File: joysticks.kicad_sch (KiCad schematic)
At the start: 27 parts, among them J1 DB9_Male_MountingHoles, J2 DB9_Male_MountingHoles, J25 Joystick Ports Mezannine Lower, J26 Joystick Ports Mezannine Upper, SW1 SW_Push_DPDT, U10 74LS06N, U11 74LS06N, U5 74LS06N, U6 74LVC374, U7 74LVC374, U8 74LS373, U9 74LS373

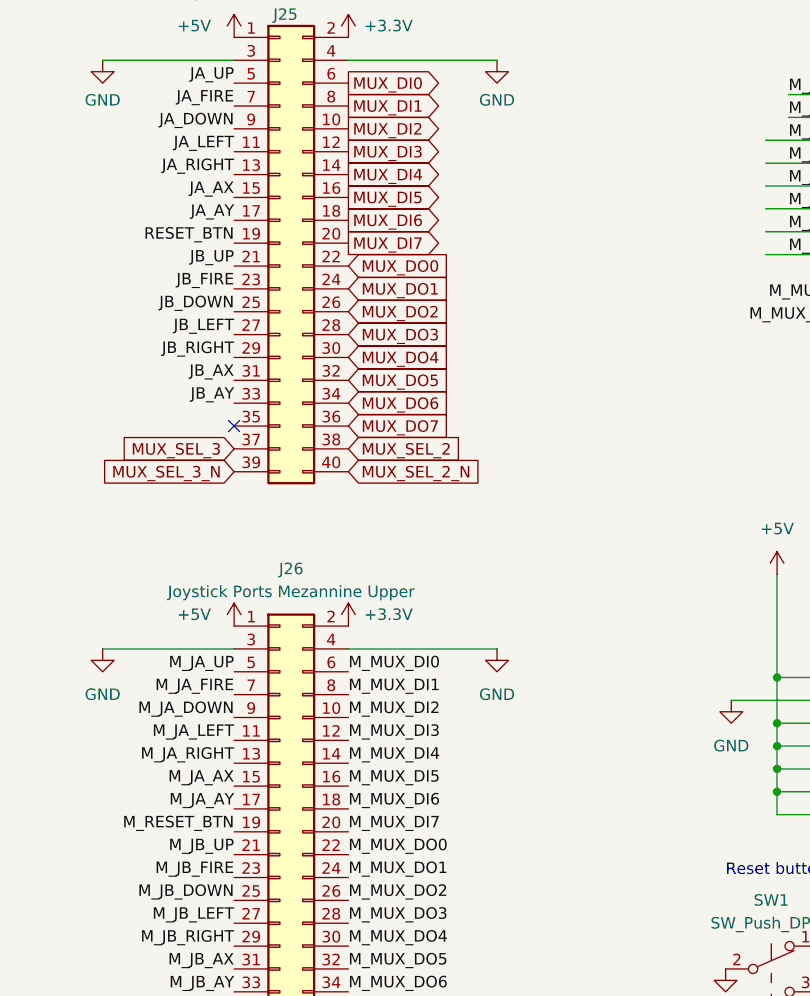
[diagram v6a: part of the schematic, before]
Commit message: finish laying out joystick mezzannine PCB
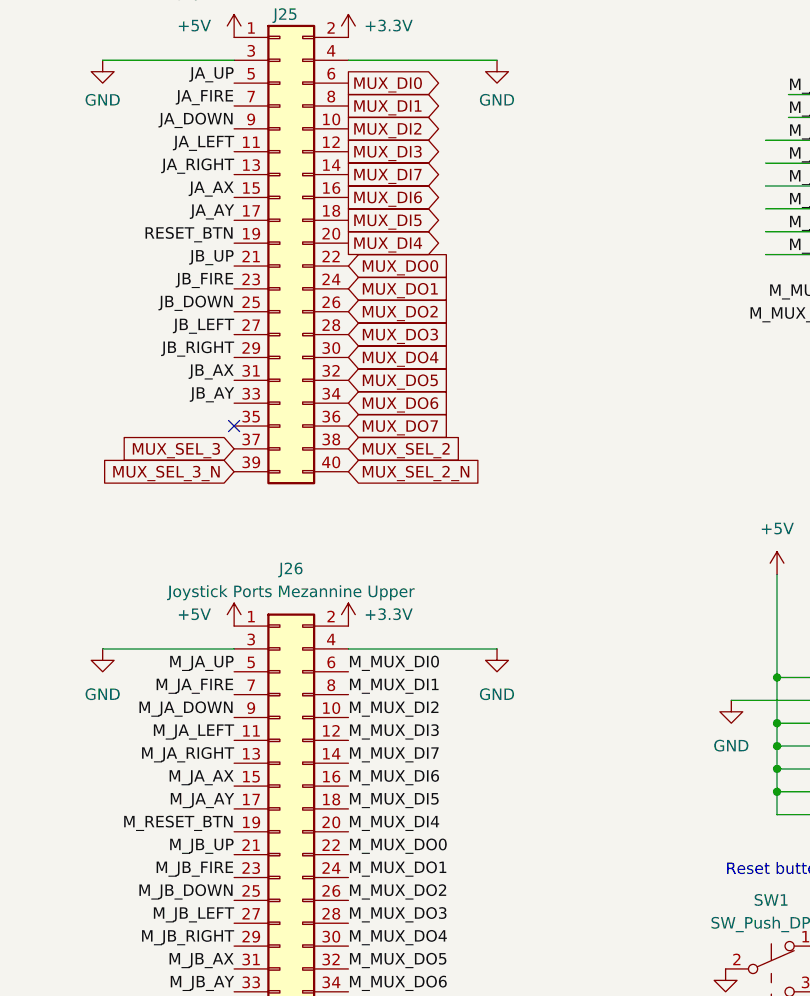
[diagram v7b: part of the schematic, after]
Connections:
- net MUX_DI4: now also J25.20 (Pin_20); no longer J25.14 (Pin_14)
- net MUX_DI5: now also J25.18 (Pin_18); no longer J25.16 (Pin_16)
- net MUX_DI6: now also J25.16 (Pin_16); no longer J25.18 (Pin_18)
- net MUX_DI7: now also J25.14 (Pin_14); no longer J25.20 (Pin_20)
- net M_MUX_DI4: now also J26.20 (Pin_20); no longer J26.14 (Pin_14)
- net M_MUX_DI5: now also J26.18 (Pin_18); no longer J26.16 (Pin_16)
- net M_MUX_DI6: now also J26.16 (Pin_16); no longer J26.18 (Pin_18)
- net M_MUX_DI7: now also J26.14 (Pin_14); no longer J26.20 (Pin_20)
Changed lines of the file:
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@@
     (effects (font (size 1.27 1.27)) (justify left bottom))
   )
-  (label "M_MUX_DI6" (at 62.23 106.68 0)
+  (label "M_MUX_DI6" (at 62.23 104.14 0)
     (effects (font (size 1.27 1.27)) (justify left bottom))
   )
@@
     (effects (font (size 1.27 1.27)) (justify left bottom))
   )
-  (label "M_MUX_DI7" (at 62.23 109.22 0)
+  (label "M_MUX_DI7" (at 62.23 101.6 0)
     (effects (font (size 1.27 1.27)) (justify left bottom))
   )
@@
     (effects (font (size 1.27 1.27)) (justify right bottom))
   )
-  (label "M_MUX_DI4" (at 62.23 101.6 0)
+  (label "M_MUX_DI4" (at 62.23 109.22 0)
     (effects (font (size 1.27 1.27)) (justify left bottom))
   )
@@
     (effects (font (size 1.27 1.27)) (justify left bottom))
   )
-  (label "M_MUX_DI5" (at 62.23 104.14 0)
+  (label "M_MUX_DI5" (at 62.23 106.68 0)
     (effects (font (size 1.27 1.27)) (justify left bottom))
   )
@@
     )
   )
-  (global_label "MUX_DI4" (shape output) (at 62.23 36.195 0) (fields_autoplaced)
-    (effects (font (size 1.27 1.27)) (justify left))
-    (property "Intersheet References" "${INTERSHEET_REFS}" (id 0) (at 72.6864 36.1156 0)
+  (global_label "MUX_DI4" (shape output) (at 62.23 43.815 0) (fields_autoplaced)
+    (effects (font (size 1.27 1.27)) (justify left))
+    (property "Intersheet References" "${INTERSHEET_REFS}" (id 0) (at 72.6864 43.8944 0)
       (effects (font (size 1.27 1.27)) (justify left) hide)
     )
@@
     )
   )
-  (global_label "MUX_DI7" (shape output) (at 62.23 43.815 0) (fields_autoplaced)
-    (effects (font (size 1.27 1.27)) (justify left))
-    (property "Intersheet References" "${INTERSHEET_REFS}" (id 0) (at 72.6864 43.7356 0)
+  (global_label "MUX_DI7" (shape output) (at 62.23 36.195 0) (fields_autoplaced)
+    (effects (font (size 1.27 1.27)) (justify left))
+    (property "Intersheet References" "${INTERSHEET_REFS}" (id 0) (at 72.6864 36.2744 0)
       (effects (font (size 1.27 1.27)) (justify left) hide)
     )
@@
     )
   )
-  (global_label "MUX_DI6" (shape output) (at 62.23 41.275 0) (fields_autoplaced)
-    (effects (font (size 1.27 1.27)) (justify left))
-    (property "Intersheet References" "${INTERSHEET_REFS}" (id 0) (at 72.6864 41.1956 0)
+  (global_label "MUX_DI6" (shape output) (at 62.23 38.735 0) (fields_autoplaced)
+    (effects (font (size 1.27 1.27)) (justify left))
+    (property "Intersheet References" "${INTERSHEET_REFS}" (id 0) (at 72.6864 38.8144 0)
       (effects (font (size 1.27 1.27)) (justify left) hide)
     )
@@
     )
   )
-  (global_label "MUX_DI5" (shape output) (at 62.23 38.735 0) (fields_autoplaced)
-    (effects (font (size 1.27 1.27)) (justify left))
-    (property "Intersheet References" "${INTERSHEET_REFS}" (id 0) (at 72.6864 38.6556 0)
-      (effects (font (size 1.27 1.27)) (justify left) hide)
-    )
+  (global_label "MUX_DI5" (shape output) (at 62.23 41.275 0) (fields_autoplaced)
+    (effects (font (size 1.27 1.27)) (justify left))
+    (property "Intersheet References" "${INTERSHEET_REFS}" (id 0) (at 72.6864 41.3544 0)
+      (effects (font (size 1.27 1.27)) (justify left) hide)
+    )

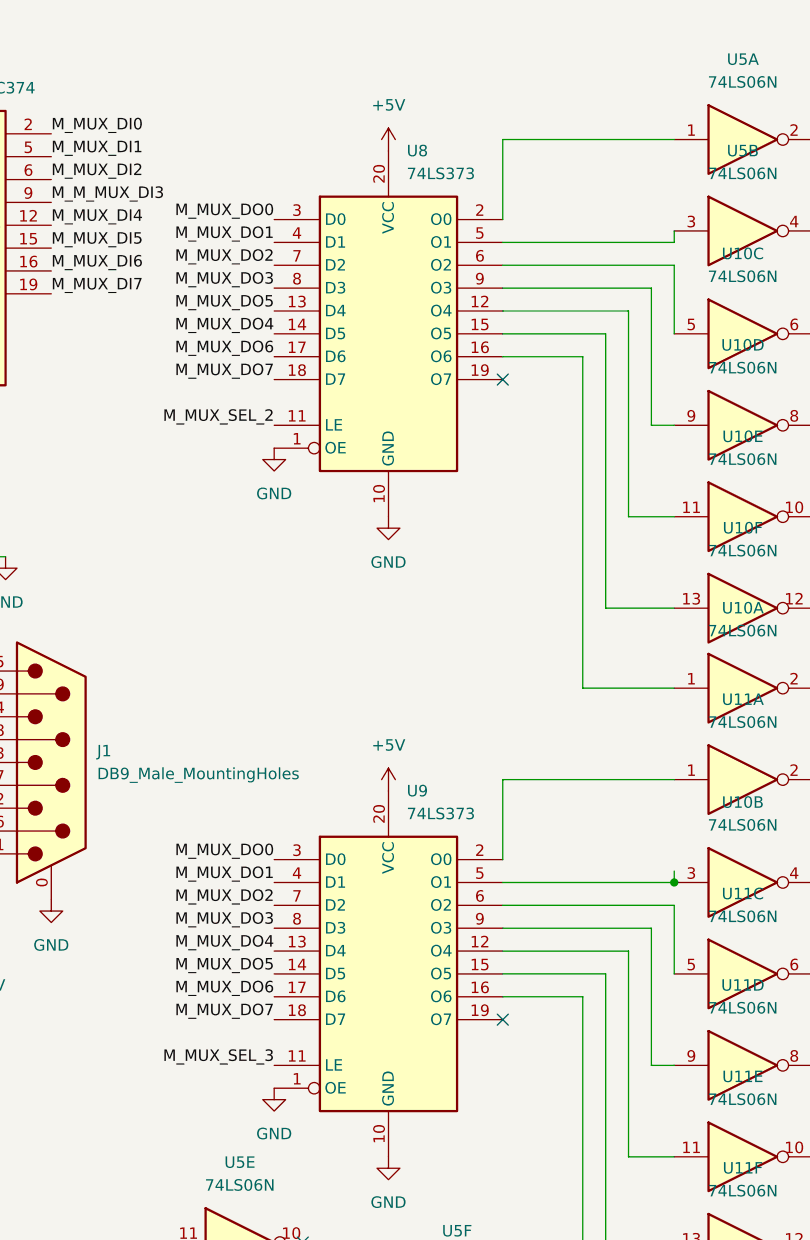
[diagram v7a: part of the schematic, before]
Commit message: replace remaining 74LS373 with 74LS374s #5
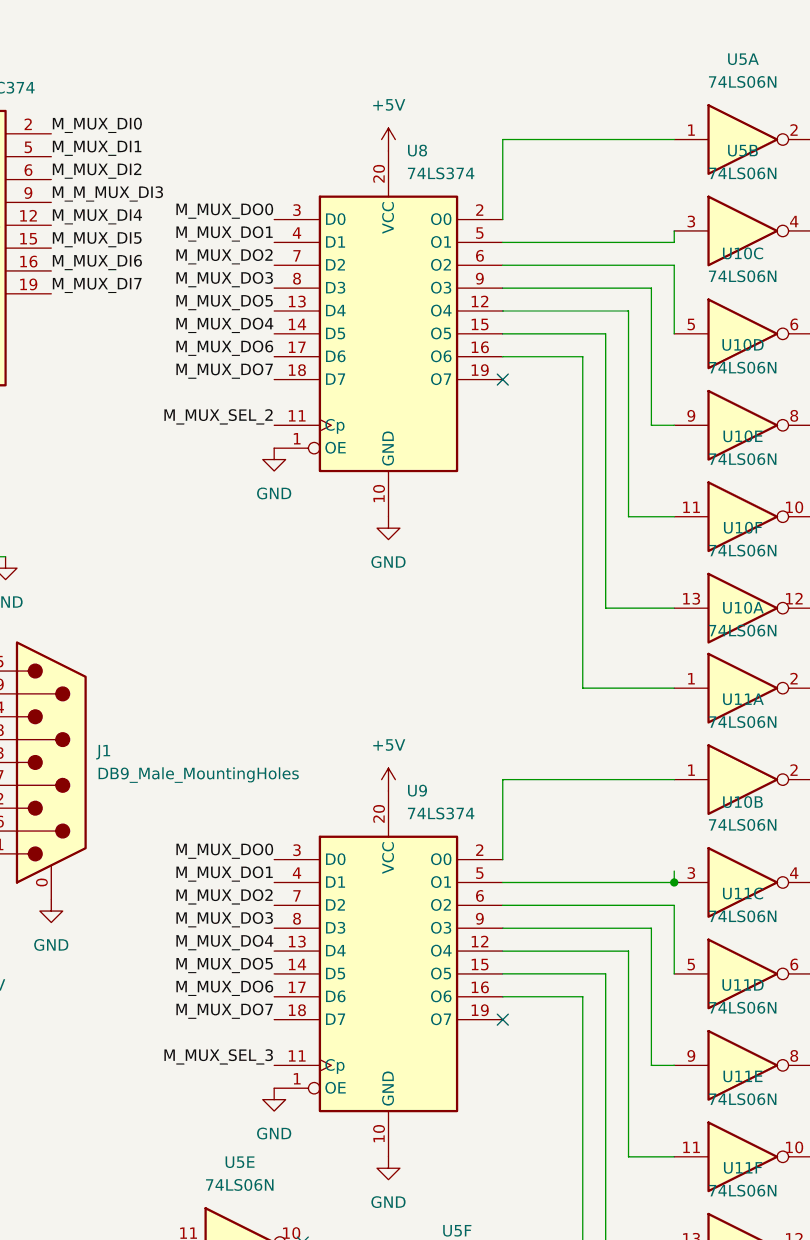
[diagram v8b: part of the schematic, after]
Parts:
- removed U8, U9: 74LS373, Package_DIP:DIP-20_W7.62mm, symbol 74xx:74LS373
- added U8, U9: 74LS374, Package_DIP:DIP-20_W7.62mm, symbol 74xx:74LS374
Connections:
- net +5V: now also U8.20 (VCC), U9.20 (VCC)
- net GND: now also U8.1 (OE), U8.10 (GND), U9.1 (OE), U9.10 (GND)
- net M_MUX_DO0: now also U8.3 (D0), U9.3 (D0)
- net M_MUX_DO1: now also U8.4 (D1), U9.4 (D1)
- net M_MUX_DO2: now also U8.7 (D2), U9.7 (D2)
- net M_MUX_DO3: now also U8.8 (D3), U9.8 (D3)
- net M_MUX_DO4: now also U8.14 (D5), U9.13 (D4)
- net M_MUX_DO5: now also U8.13 (D4), U9.14 (D5)
- net M_MUX_DO6: now also U8.17 (D6), U9.17 (D6)
- net M_MUX_DO7: now also U8.18 (D7), U9.18 (D7)
- net M_MUX_SEL_2: now also U8.11 (Cp)
- net M_MUX_SEL_3: now also U9.11 (Cp)
- net at U5.1: now also U8.2 (O0)
- net at U10.3: now also U9.5 (O1)
- net at U10.11: now also U8.12 (O4)
- net at U11.11: now also U9.12 (O4)
- net at U11.13: now also U9.15 (O5)
- net at U11.3: now also U9.16 (O6)
- net at U11.1: now also U9.2 (O0)
- net at U11.5: now also U9.6 (O2)
- net at U11.9: now also U9.9 (O3)
- net at U10.1: now also U8.16 (O6)
- net at U10.13: now also U8.15 (O5)
- net at U5.3: now also U8.5 (O1)
- net at U10.5: now also U8.6 (O2)
- net at U10.9: now also U8.9 (O3)
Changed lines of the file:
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@@
     (pin "2")
-  )
-  (symbol (lib_id "74xx:74LS373") (at 184.15 120.65 0) (unit 1)
-    (in_bom yes) (on_board yes) (fields_autoplaced)
-    (property "Reference" "U9" (id 0) (at 186.1694 100.33 0)
-      (effects (font (size 1.27 1.27)) (justify left))
-    )
-    (property "Value" "74LS373" (id 1) (at 186.1694 102.87 0)
-      (effects (font (size 1.27 1.27)) (justify left))
-    )
-    (property "Footprint" "Package_DIP:DIP-20_W7.62mm" (id 2) (at 184.15 120.65 0)
-      (effects (font (size 1.27 1.27)) hide)
-    )
-    (property "Datasheet" "http://www.ti.com/lit/gpn/sn74LS373" (id 3) (at 184.15 120.65 0)
-      (effects (font (size 1.27 1.27)) hide)
-    )
-    (pin "1")
-    (pin "10")
-    (pin "11")
-    (pin "12")
-    (pin "13")
-    (pin "14")
-    (pin "15")
-    (pin "16")
-    (pin "17")
-    (pin "18")
-    (pin "19")
-    (pin "2")
-    (pin "20")
-    (pin "3")
-    (pin "4")
-    (pin "5")
-    (pin "6")
-    (pin "7")
-    (pin "8")
-    (pin "9")
   )
   (symbol (lib_id "power:+5V") (at 252.095 41.91 90) (unit 1)
@@
     (pin "13")
   )
-  (symbol (lib_id "74xx:74LS373") (at 184.15 49.53 0) (unit 1)
+  (symbol (lib_id "74xx:74LS06N") (at 167.64 163.195 0) (unit 4)
+    (in_bom yes) (on_board yes) (fields_autoplaced)
+    (property "Reference" "U5" (id 0) (at 167.64 154.305 0))
+    (property "Value" "74LS06N" (id 1) (at 167.64 156.845 0))
+    (property "Footprint" "Package_DIP:DIP-14_W7.62mm" (id 2) (at 167.64 163.195 0)
+      (effects (font (size 1.27 1.27)) hide)
+    )
+    (property "Datasheet" "http://www.ti.com/lit/gpn/sn74LS06N" (id 3) (at 167.64 163.195 0)
+      (effects (font (size 1.27 1.27)) hide)
+    )
+    (pin "8")
+    (pin "9")
+  )
+  (symbol (lib_id "pspice:R") (at 120.015 107.315 90) (unit 1)
+    (in_bom yes) (on_board yes)
+    (property "Reference" "R21" (id 0) (at 125.095 106.045 90))
+    (property "Value" "4K7" (id 1) (at 120.015 107.315 90))
+    (property "Footprint" "Resistor_THT:R_Box_L8.4mm_W2.5mm_P5.08mm" (id 2) (at 120.015 107.315 0)
+      (effects (font (size 1.27 1.27)) hide)
+    )
+    (property "Datasheet" "~" (id 3) (at 120.015 107.315 0)
+      (effects (font (size 1.27 1.27)) hide)
+    )
+    (pin "1")
+    (pin "2")
+  )
+  (symbol (lib_id "74xx:74LS06N") (at 264.795 59.69 90) (unit 7)
+    (in_bom yes) (on_board yes) (fields_autoplaced)
+    (property "Reference" "U10" (id 0) (at 264.795 48.895 90))
+    (property "Value" "74LS06N" (id 1) (at 264.795 51.435 90))
+    (property "Footprint" "Package_DIP:DIP-14_W7.62mm" (id 2) (at 264.795 59.69 0)
+      (effects (font (size 1.27 1.27)) hide)
+    )
+    (property "Datasheet" "http://www.ti.com/lit/gpn/sn74LS06N" (id 3) (at 264.795 59.69 0)
+      (effects (font (size 1.27 1.27)) hide)
+    )
+    (pin "14")
+    (pin "7")
+  )
+  (symbol (lib_id "74xx:74LS374") (at 184.15 49.53 0) (unit 1)
     (in_bom yes) (on_board yes) (fields_autoplaced)
     (property "Reference" "U8" (id 0) (at 186.1694 29.21 0)
       (effects (font (size 1.27 1.27)) (justify left))
     )
-    (property "Value" "74LS373" (id 1) (at 186.1694 31.75 0)
+    (property "Value" "74LS374" (id 1) (at 186.1694 31.75 0)
       (effects (font (size 1.27 1.27)) (justify left))
     )
@@
       (effects (font (size 1.27 1.27)) hide)
     )
-    (property "Datasheet" "http://www.ti.com/lit/gpn/sn74LS373" (id 3) (at 184.15 49.53 0)
+    (property "Datasheet" "http://www.ti.com/lit/gpn/sn74LS374" (id 3) (at 184.15 49.53 0)
       (effects (font (size 1.27 1.27)) hide)
     )
@@
     (pin "9")
   )
-  (symbol (lib_id "74xx:74LS06N") (at 167.64 163.195 0) (unit 4)
-    (in_bom yes) (on_board yes) (fields_autoplaced)
-    (property "Reference" "U5" (id 0) (at 167.64 154.305 0))
-    (property "Value" "74LS06N" (id 1) (at 167.64 156.845 0))
-    (property "Footprint" "Package_DIP:DIP-14_W7.62mm" (id 2) (at 167.64 163.195 0)
-      (effects (font (size 1.27 1.27)) hide)
-    )
-    (property "Datasheet" "http://www.ti.com/lit/gpn/sn74LS06N" (id 3) (at 167.64 163.195 0)
-      (effects (font (size 1.27 1.27)) hide)
-    )
-    (pin "8")
-    (pin "9")
-  )
-  (symbol (lib_id "pspice:R") (at 120.015 107.315 90) (unit 1)
-    (in_bom yes) (on_board yes)
-    (property "Reference" "R21" (id 0) (at 125.095 106.045 90))
-    (property "Value" "4K7" (id 1) (at 120.015 107.315 90))
-    (property "Footprint" "Resistor_THT:R_Box_L8.4mm_W2.5mm_P5.08mm" (id 2) (at 120.015 107.315 0)
-      (effects (font (size 1.27 1.27)) hide)
-    )
-    (property "Datasheet" "~" (id 3) (at 120.015 107.315 0)
-      (effects (font (size 1.27 1.27)) hide)
-    )
-    (pin "1")
-    (pin "2")
-  )
-  (symbol (lib_id "74xx:74LS06N") (at 264.795 59.69 90) (unit 7)
-    (in_bom yes) (on_board yes) (fields_autoplaced)
-    (property "Reference" "U10" (id 0) (at 264.795 48.895 90))
-    (property "Value" "74LS06N" (id 1) (at 264.795 51.435 90))
-    (property "Footprint" "Package_DIP:DIP-14_W7.62mm" (id 2) (at 264.795 59.69 0)
-      (effects (font (size 1.27 1.27)) hide)
-    )
-    (property "Datasheet" "http://www.ti.com/lit/gpn/sn74LS06N" (id 3) (at 264.795 59.69 0)
-      (effects (font (size 1.27 1.27)) hide)
-    )
-    (pin "14")
-    (pin "7")
-  )
   (symbol (lib_id "power:GND") (at 277.495 41.91 90) (unit 1)
     (in_bom yes) (on_board yes) (fields_autoplaced)
@@
     (pin "1")
   )
+  (symbol (lib_id "74xx:74LS374") (at 184.15 120.65 0) (unit 1)
+    (in_bom yes) (on_board yes) (fields_autoplaced)
+    (property "Reference" "U9" (id 0) (at 186.1694 100.33 0)
+      (effects (font (size 1.27 1.27)) (justify left))
+    )
+    (property "Value" "74LS374" (id 1) (at 186.1694 102.87 0)
+      (effects (font (size 1.27 1.27)) (justify left))
+    )
+    (property "Footprint" "Package_DIP:DIP-20_W7.62mm" (id 2) (at 184.15 120.65 0)
+      (effects (font (size 1.27 1.27)) hide)
+    )
+    (property "Datasheet" "http://www.ti.com/lit/gpn/sn74LS374" (id 3) (at 184.15 120.65 0)
+      (effects (font (size 1.27 1.27)) hide)
+    )
+    (pin "1")
+    (pin "10")
+    (pin "11")
+    (pin "12")
+    (pin "13")
+    (pin "14")
+    (pin "15")
+    (pin "16")
+    (pin "17")
+    (pin "18")
+    (pin "19")
+    (pin "2")
+    (pin "20")
+    (pin "3")
+    (pin "4")
+    (pin "5")
+    (pin "6")
+    (pin "7")
+    (pin "8")
+    (pin "9")
+  )
 )
